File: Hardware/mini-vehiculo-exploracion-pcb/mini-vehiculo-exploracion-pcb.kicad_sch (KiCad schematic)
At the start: 22 parts, among them J1 ArducamMINIOV2640, U1 BNO086, U2 ESP32-S3-WROOM-1, U3 DRV8873HPWPRQ1, U4 DRV8873HPWPRQ1

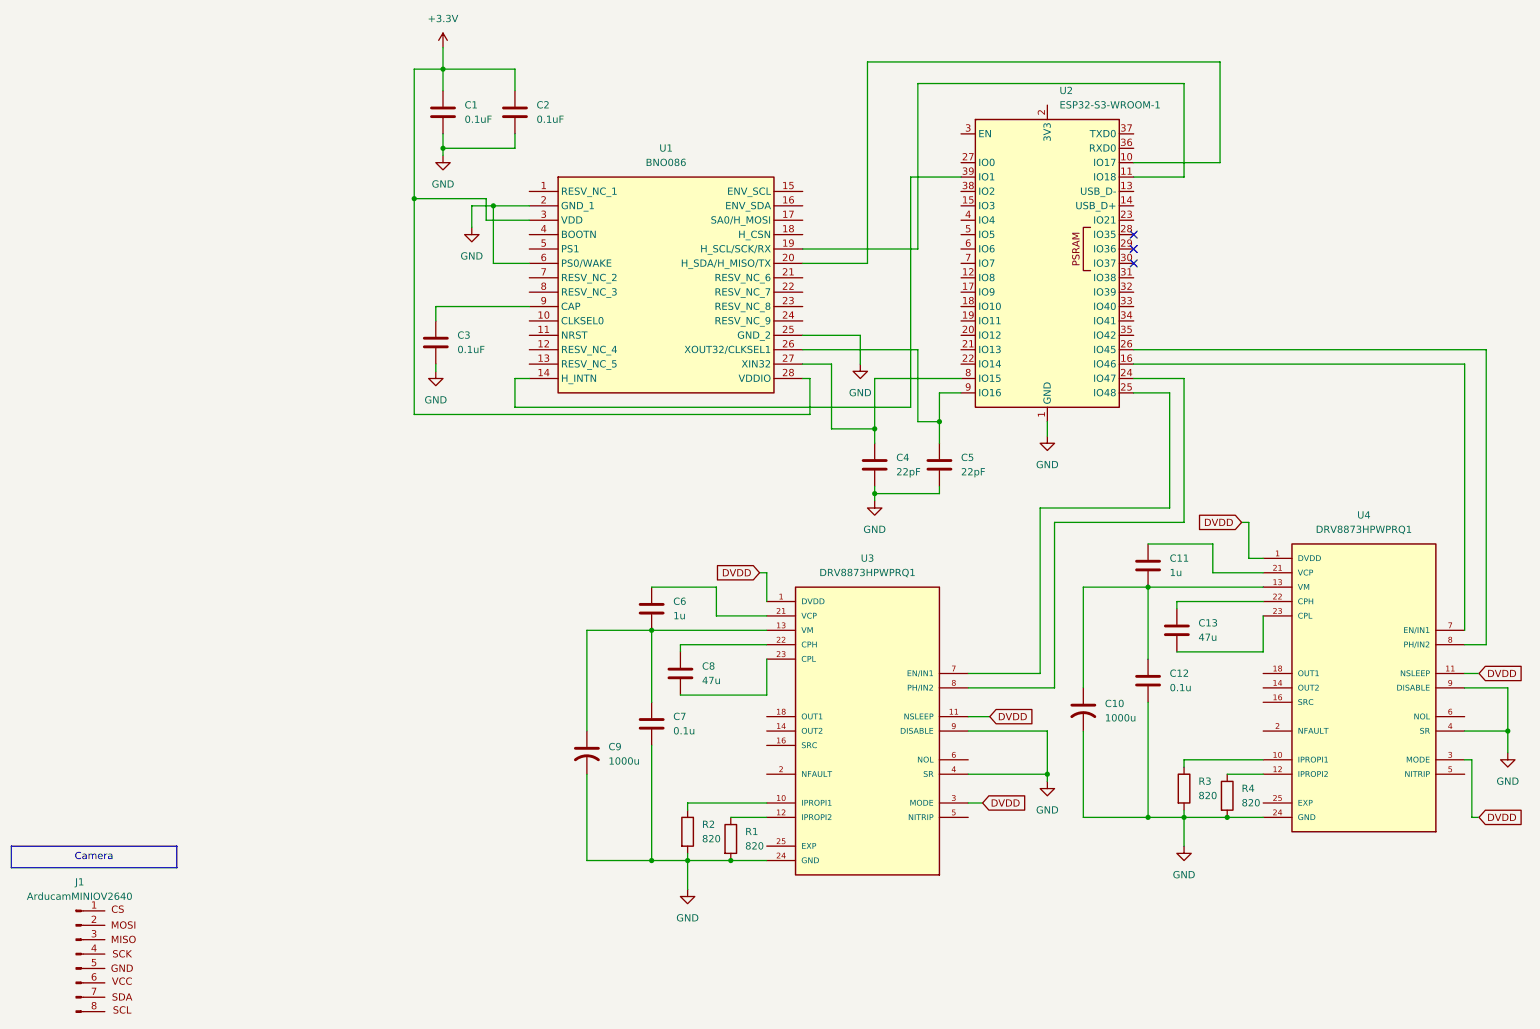
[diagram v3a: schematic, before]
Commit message: Fixing labels
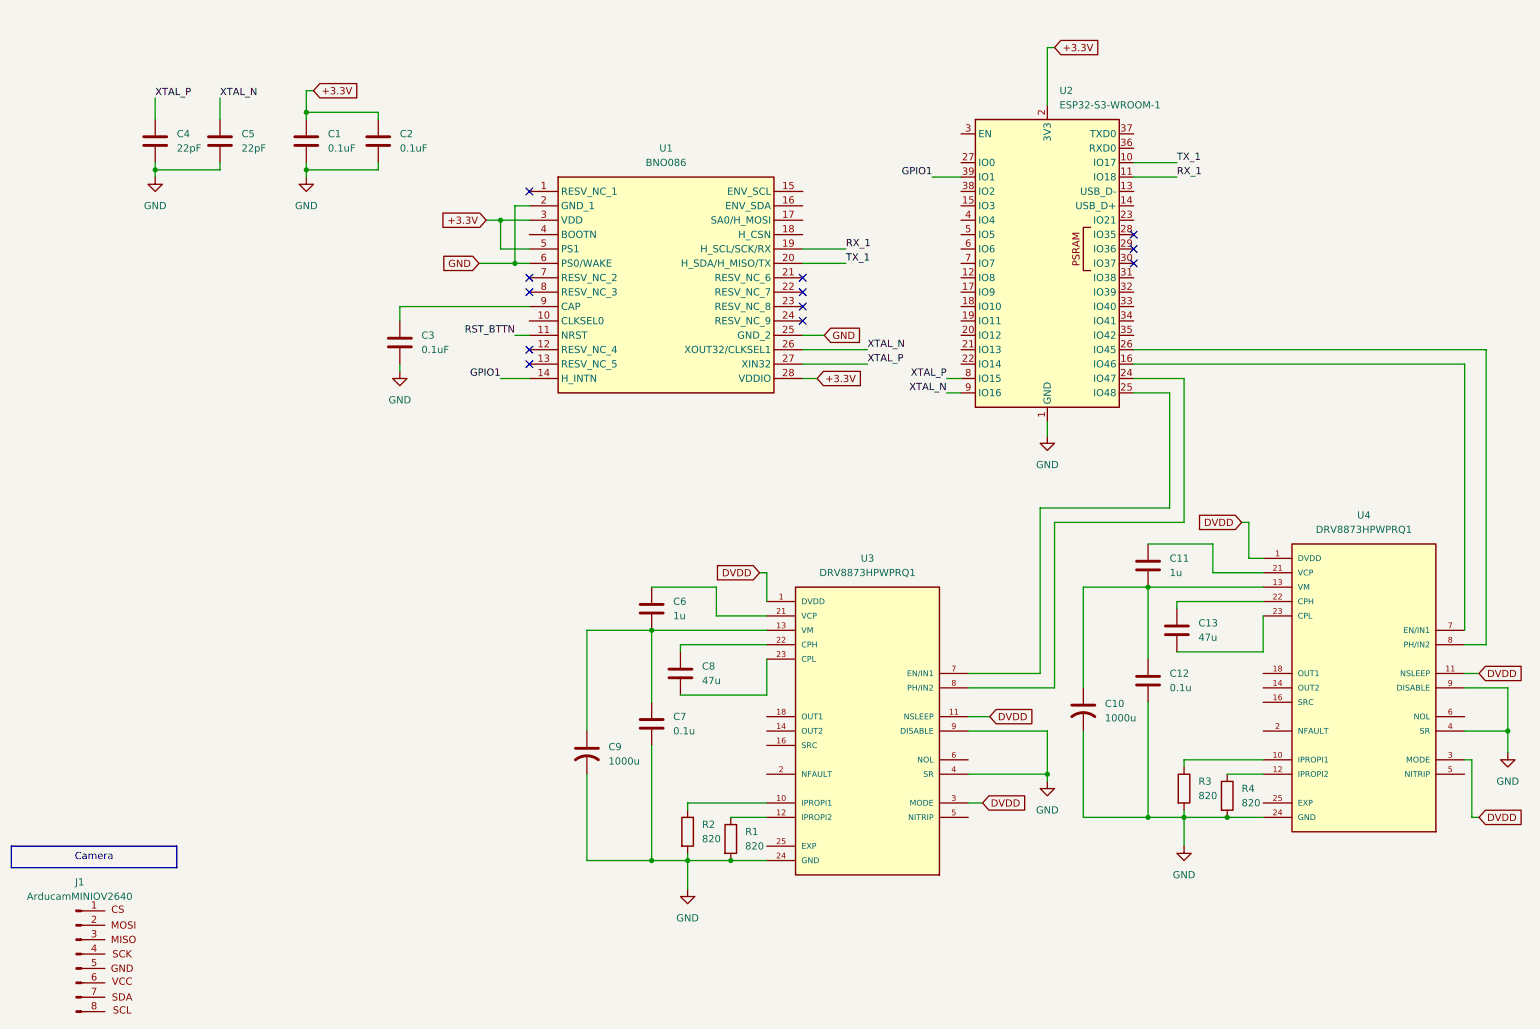
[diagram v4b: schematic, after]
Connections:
- net +3.3V: now also U1.5 (PS1), U2.2 (3V3)
- net XTAL_N: now reaches C5.1, U1.26 (XOUT32/CLKSEL1), U2.9 (IO16)
- net TX_1: now reaches U1.20 (H_SDA/H_MISO/TX), U2.10 (IO17)
- net RX_1: now reaches U1.19 (H_SCL/SCK/RX), U2.11 (IO18)
- net GPIO1: now reaches U1.14 (H_INTN), U2.39 (IO1)
- net XTAL_P: now reaches C4.1, U1.27 (XIN32), U2.8 (IO15)
- net RST_BTTN: now reaches U1.11 (NRST)
- no-connect marks 3 -> 12
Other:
- moved on the sheet: C1, C2, C3, C4, C5

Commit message: update bno086 schematic
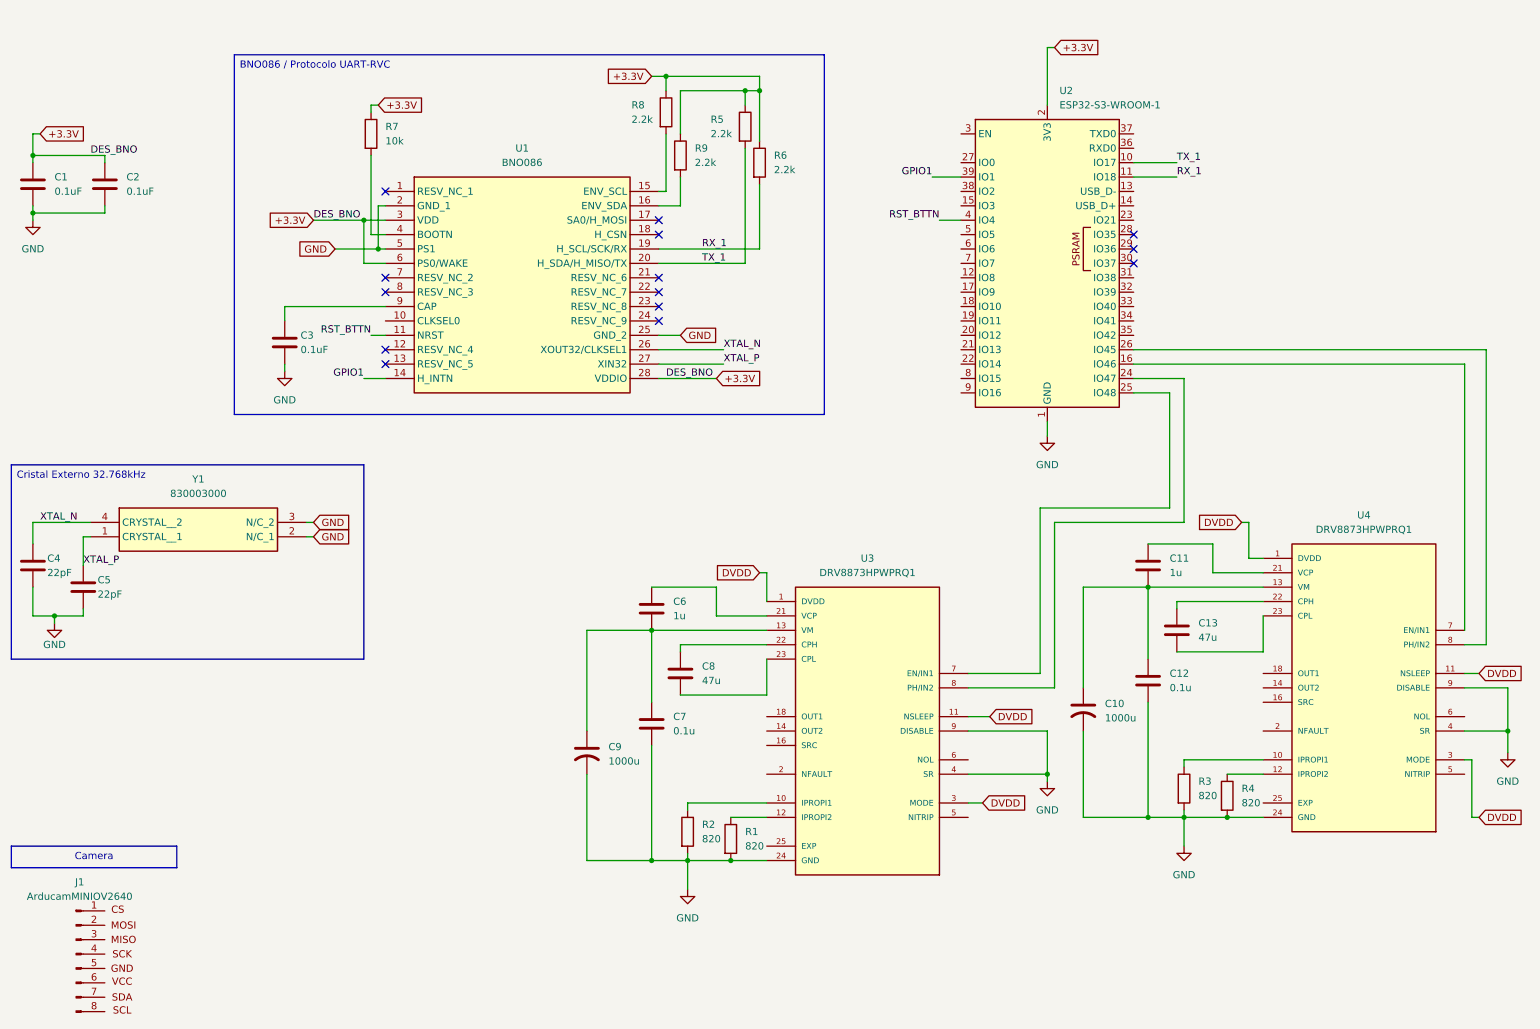
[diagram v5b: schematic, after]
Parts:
- added R5, R6, R8, R9: 2.2k, symbol Device:R
- added R7: 10k, symbol Device:R
- added Y1: 830003000, 830003000, symbol 830003000:830003000
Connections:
- net +3.3V: now also U1.6 (PS0/WAKE), R5.1, R6.1, R7.1, R8.1, R9.1; no longer U1.5 (PS1)
- net GND: now also U1.5 (PS1), Y1.2 (N/C_1), Y1.3 (N/C_2); no longer U1.6 (PS0/WAKE)
- net RST_BTTN: now also U2.4 (IO4)
- net RX_1: now also R6.2
- net TX_1: now also R5.2
- net XTAL_N: now also C4.1, Y1.4 (CRYSTAL__2); no longer C5.1, U2.9 (IO16)
- net XTAL_P: now also C5.1, Y1.1 (CRYSTAL__1); no longer C4.1, U2.8 (IO15)
- net at U1.15 (ENV_SCL): now also R8.2
- net at U1.16 (ENV_SDA): now also R9.2
- net at U1.4 (BOOTN): now also R7.2
- no-connect marks 12 -> 14
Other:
- moved on the sheet: C1, C2, C3, C4, C5, U1

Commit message: add separate driver schematic
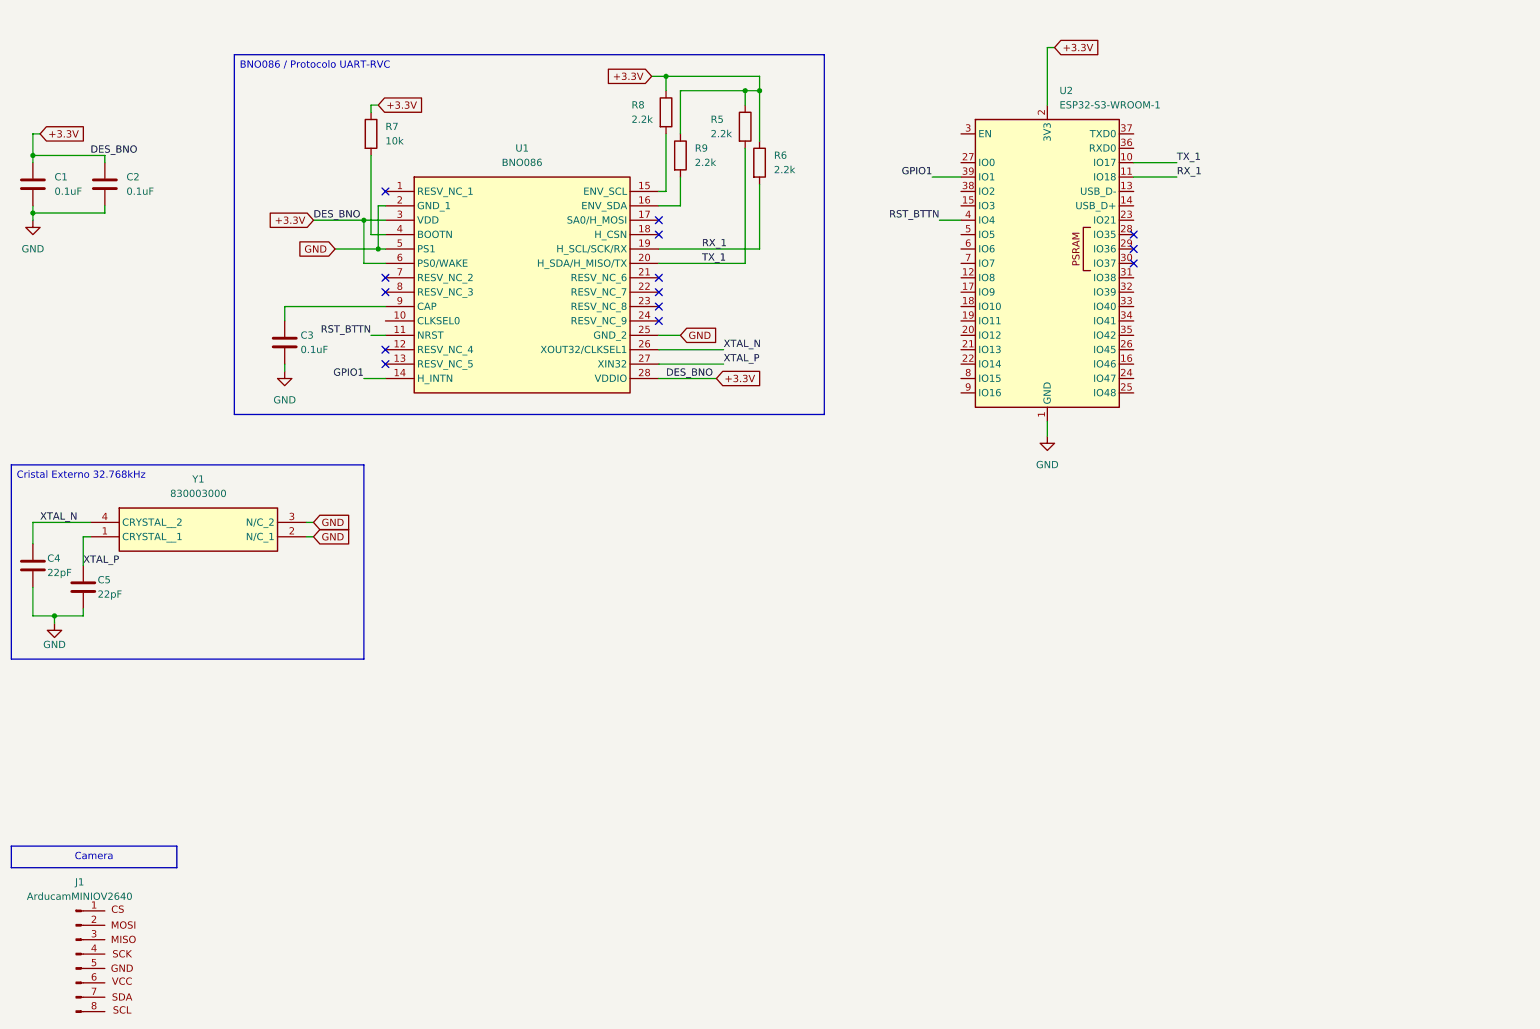
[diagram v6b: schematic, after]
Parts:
- removed C10, C9: 1000u, symbol Device:C_US
- removed C11, C6: 1u, symbol Device:C
- removed C12, C7: 0.1u, symbol Device:C
- removed C13, C8: 47u, symbol Device:C
- removed R1, R2, R3, R4: 820, symbol Device:R
- removed U3, U4: DRV8873HPWPRQ1, DRV8873HPWPRQ1:SOP65P640X120-25N, symbol DRV8873HPWPRQ1:DRV8873HPWPRQ1

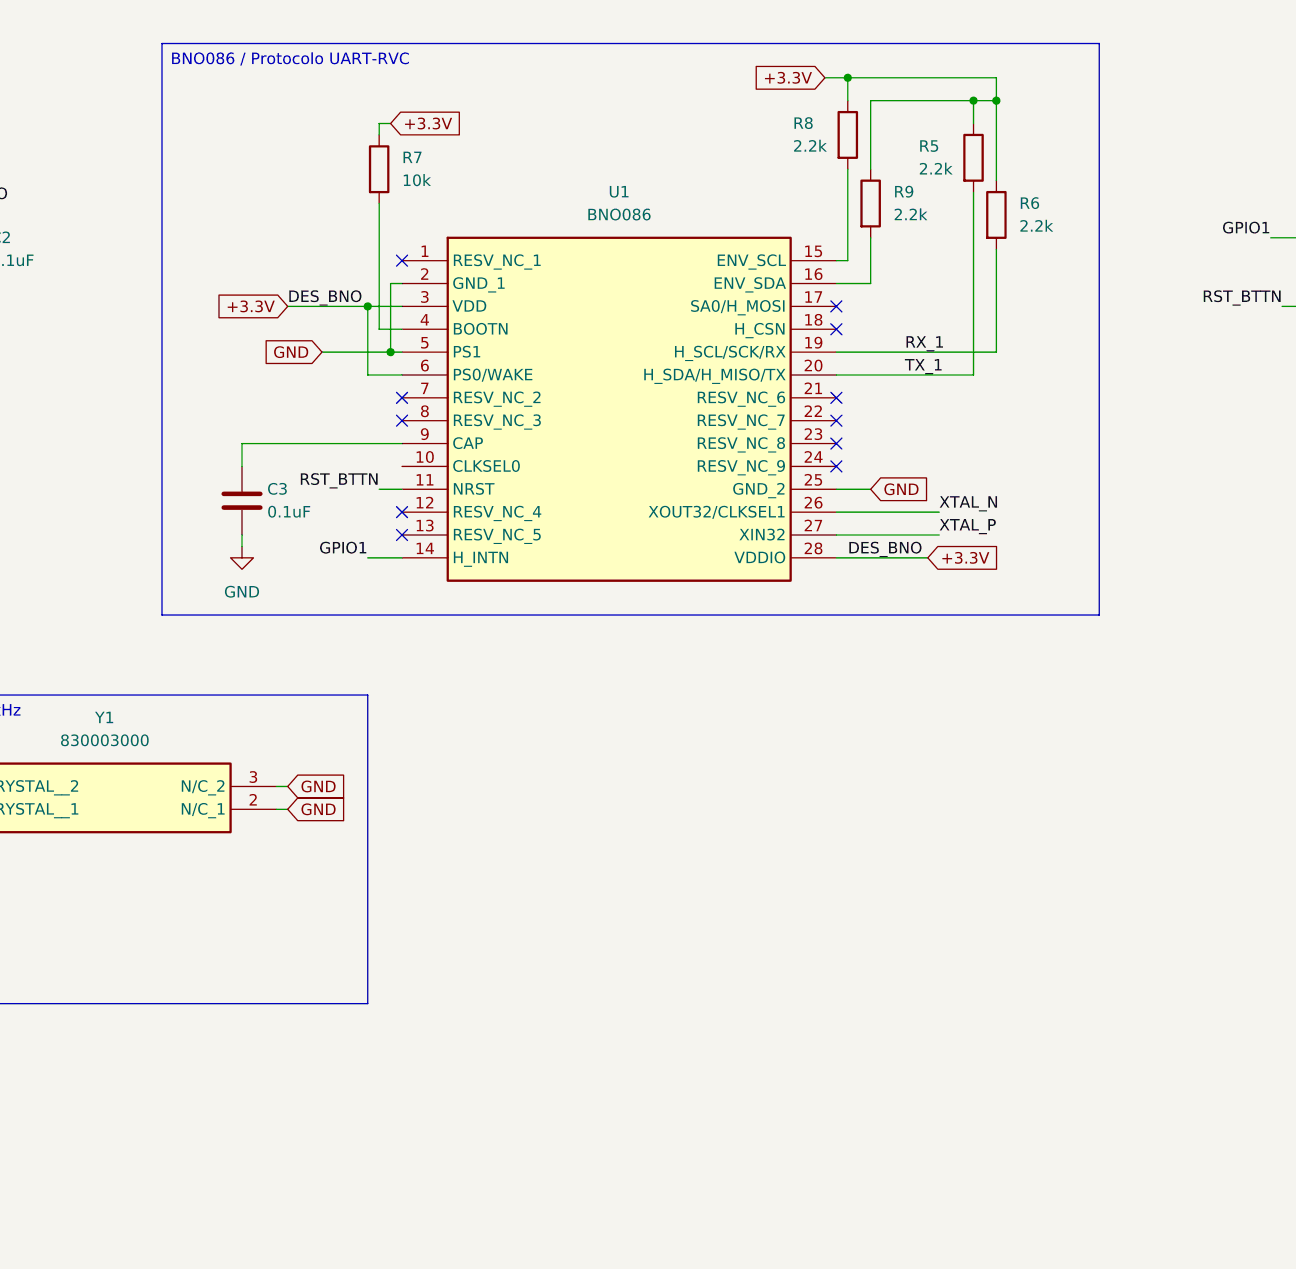
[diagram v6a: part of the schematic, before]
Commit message: add bme690
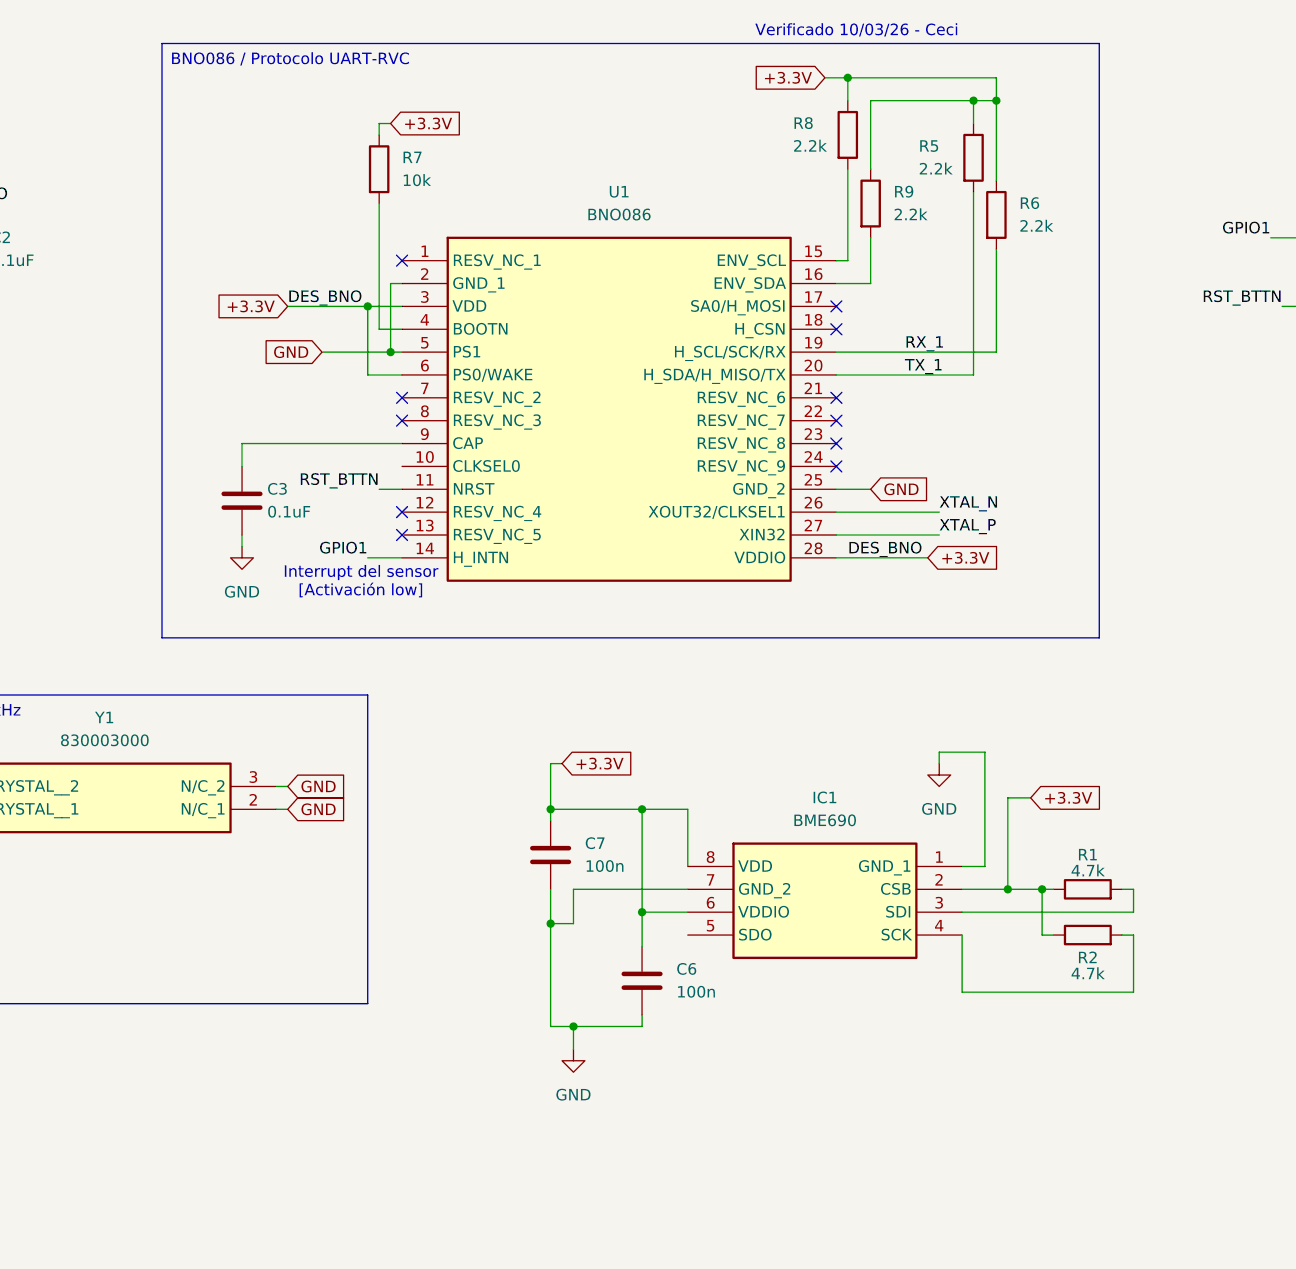
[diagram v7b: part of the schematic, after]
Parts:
- added C6, C7: 100n, symbol Device:C
- added IC1: BME690, BME690, symbol BME690:BME690
- added R1, R2: 4.7k, symbol Device:R
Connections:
- net +3.3V: now also C6.1, C7.1, IC1.2 (CSB), IC1.6 (VDDIO), IC1.8 (VDD), R1.1, R2.1
- net GND: now also C6.2, C7.2, IC1.1 (GND_1), IC1.7 (GND_2)
- new net: IC1.3 (SDI), R1.2
- new net: IC1.4 (SCK), R2.2
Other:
- note added: "Interrupt del sensor [Activación low]"
- note added: "Verificado 10/03/26 - Ceci"
